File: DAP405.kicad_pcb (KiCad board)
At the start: 2 copper layers, 64 x 39 mm, 56 parts, among them J1 USB_B, J2 Target, J3 JTAG, U1 LT1117-3.3, U10 74LVC1G17, U11 SN74LVC1T45DBV, U12 SN74LVC1T45DBV, U13 SN74LVC1T45DBV, U14 SY6280, U2 USB3300-EZK, U3 STM32F405RGTx, U4 REF3033, U5 74LVC1G17, U6 SN74LVC1T45DBV, U7 SN74LVC1T45DBV, U8 SN74LVC1T45DBV, U9 SN74LVC1T45DBV, Y1 24M, Y2 12M

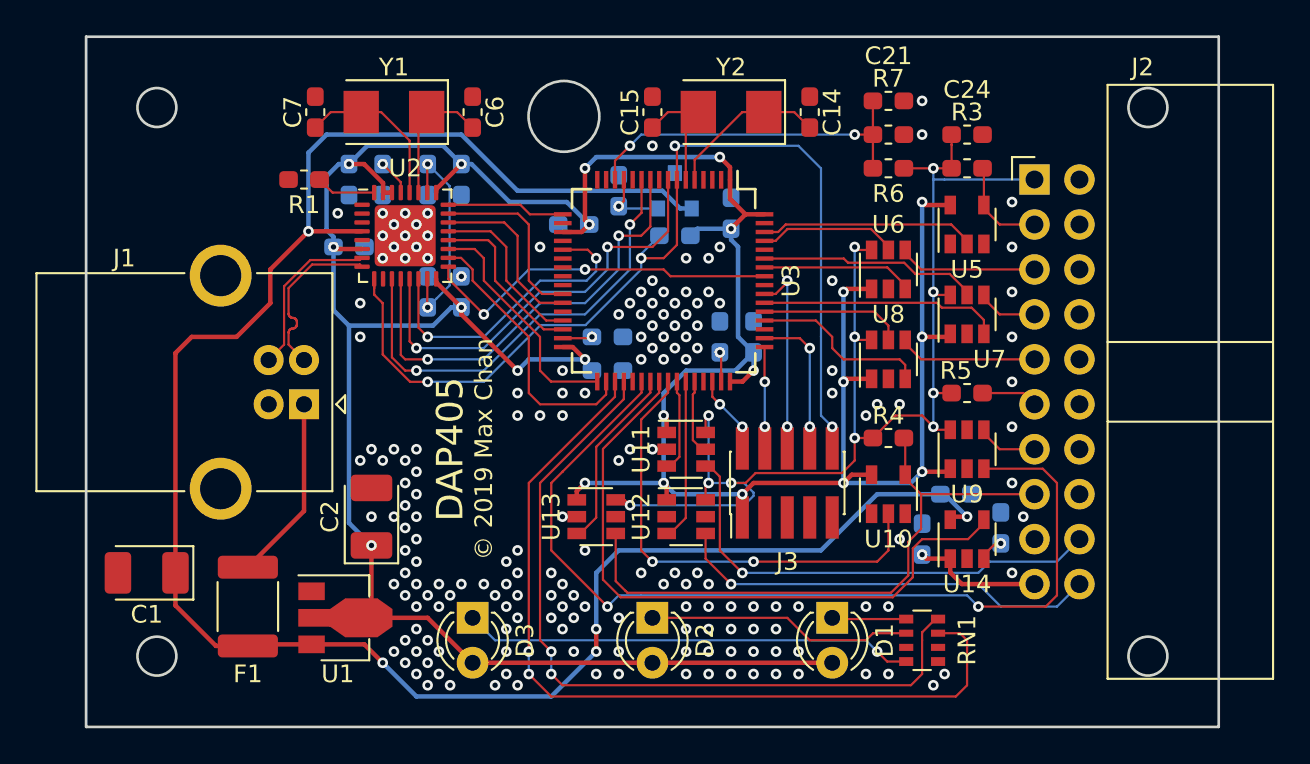
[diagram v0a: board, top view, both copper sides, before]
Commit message: Fixing the ULPI interface.
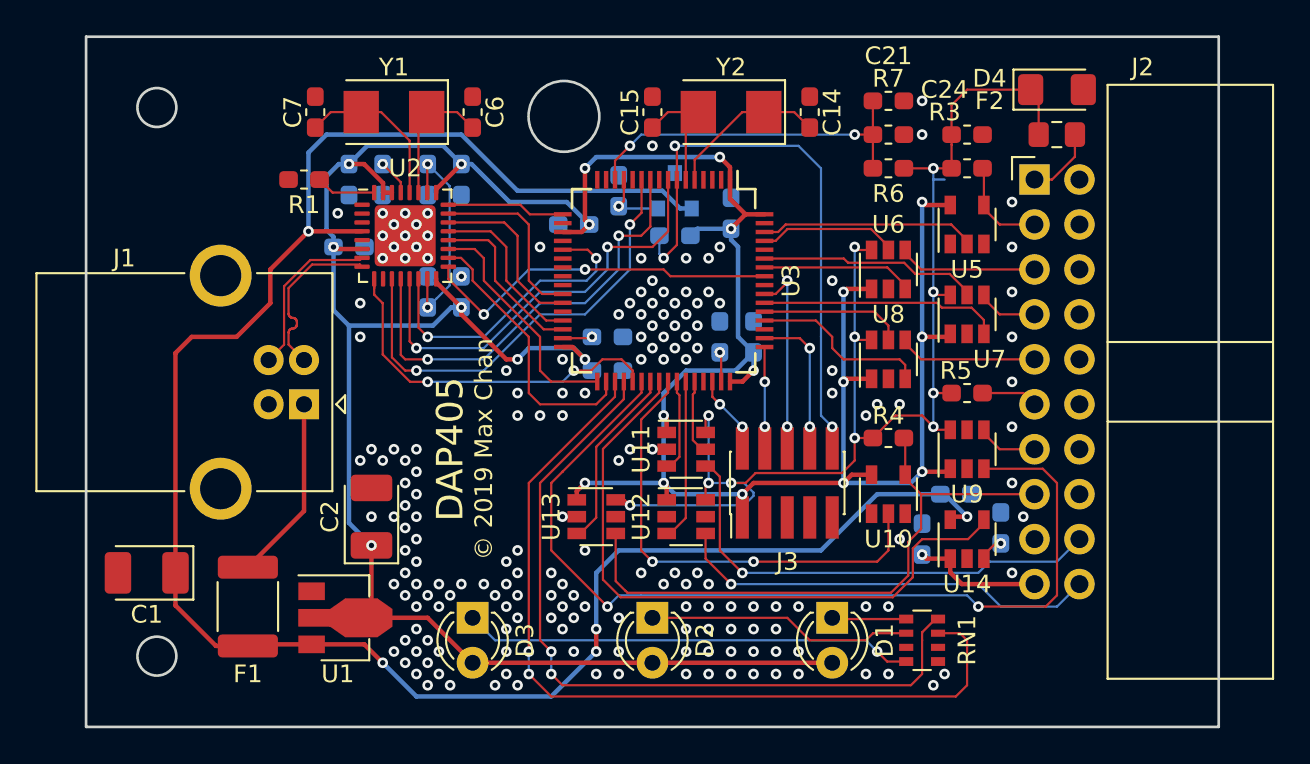
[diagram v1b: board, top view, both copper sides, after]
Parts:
- added D4: SMF5.0A, Diode_SMD:D_1206_3216Metric_Pad1.42x1.75mm_HandSolder, F.Cu at (172.9, 83.5)
- added F2: 200mA, Fuse:Fuse_0805_2012Metric_Pad1.15x1.40mm_HandSolder, F.Cu at (172.8, 86.0)
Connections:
- J2 pad 1: VDD -> Net-(F2-Pad1)
- U2 pad 9: /~RESET -> /ULPI_RST
- U3 pad 37: (no net) -> /ULPI_RST
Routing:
- net /~RESET: track 58.1 -> 33.0 mm, vias 4 -> 3
- net /ULPI_RST: track 0.00 -> 21.2 mm, vias 0 -> 2
- net VDD: track 71.8 -> 76.0 mm
- net Net-(F2-Pad1): track 0.00 -> 4.07 mm
- net GND: vias 180 -> 181
- net (no net): vias 0 -> 1
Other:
- outline, holes or cut-outs redrawn

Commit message: STM32F446 version
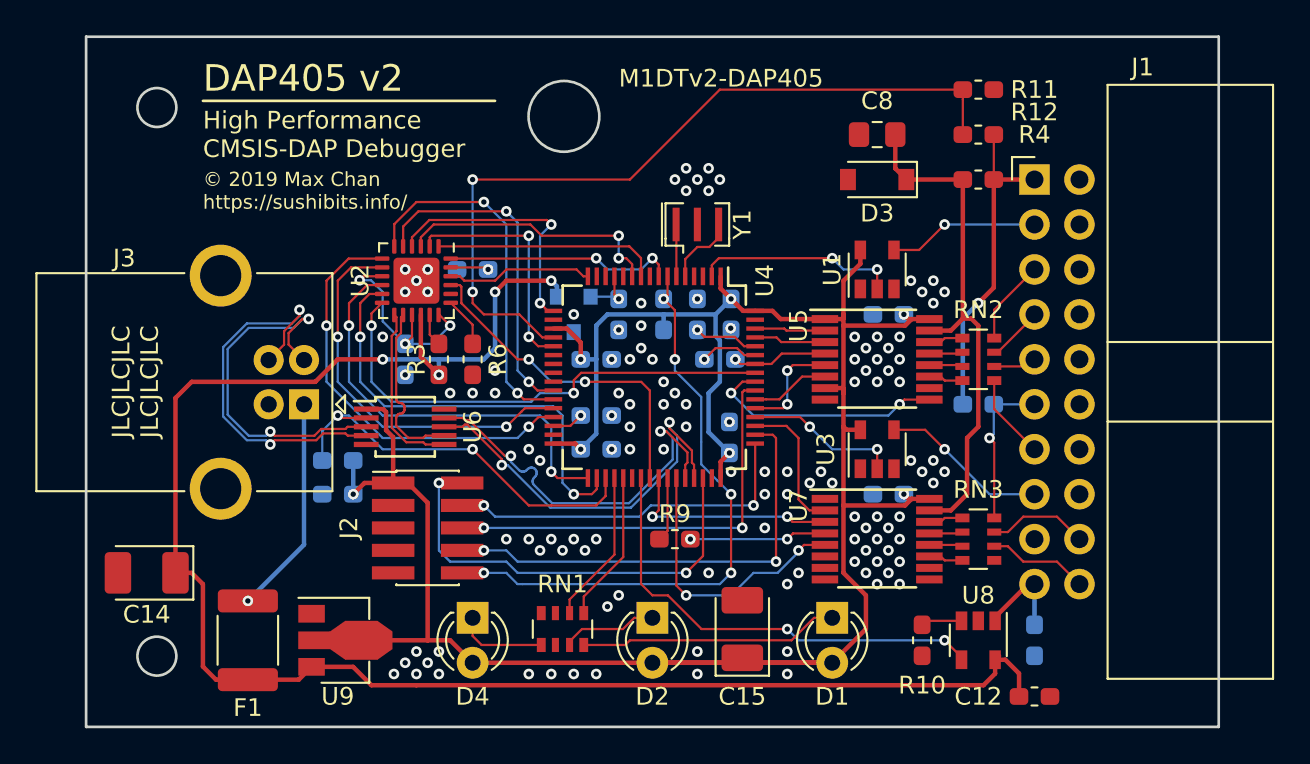
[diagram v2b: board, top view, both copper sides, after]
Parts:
- removed the C12 at (147.5, 97.5)
- removed the C13 at (153.8, 97.5)
- removed the C14 at (158.9, 84.8)
- removed the C15 at (150.0, 84.8)
- removed the C16 at (154.4, 90.5)
- removed C17, C18, C19: 100n, Capacitor_SMD:C_0603_1608Metric_Pad1.05x0.95mm_HandSolder
- removed C21, C24: 1µ, Capacitor_SMD:C_0603_1608Metric_Pad1.05x0.95mm_HandSolder
- removed the D4 at (172.9, 83.5)
- removed F2: 200mA, Fuse:Fuse_0805_2012Metric_Pad1.15x1.40mm_HandSolder
- removed the U10 at (163.3, 106.3)
- removed U11, U12, U13: SN74LVC1T45DBV, Package_TO_SOT_SMD:SOT-23-6
- removed the U8 at (163.3, 98.7)
- removed the U9 at (167.8, 103.8)
- removed Y2: 12M, Crystal:Crystal_SMD_5032-2Pin_5.0x3.2mm
- added C1: 1µ, Capacitor_SMD:C_0603_1608Metric_Pad1.05x0.95mm_HandSolder, B.Cu at (136.0, 98.7)
- added C2: 1µ, Capacitor_SMD:C_0603_1608Metric_Pad1.05x0.95mm_HandSolder, B.Cu at (139.8, 93.7)
- added D3: BZT52C3V3, Diode_SMD:D_SOD-123, F.Cu at (162.7, 88.6)
- added R11: 20k, Resistor_SMD:R_0603_1608Metric_Pad1.05x0.95mm_HandSolder, F.Cu at (168.4, 86.0)
- added R12: 30k, Resistor_SMD:R_0603_1608Metric_Pad1.05x0.95mm_HandSolder, F.Cu at (168.4, 83.5)
- added R8: 510, Resistor_SMD:R_0603_1608Metric_Pad1.05x0.95mm_HandSolder, B.Cu at (153.8, 98.7)
- added R9: 510, Resistor_SMD:R_0603_1608Metric_Pad1.05x0.95mm_HandSolder, F.Cu at (151.3, 108.9)
- added RN2: 220, Resistor_SMD:R_Array_Convex_4x0603, F.Cu at (168.4, 98.7)
- added RN3: 220, Resistor_SMD:R_Array_Convex_4x0603, F.Cu at (168.4, 108.9)
- added U1: 74LVC1G07, Package_TO_SOT_SMD:SOT-23-5, F.Cu at (162.7, 93.7)
- added U4: STM32F446RCTx, Package_QFP:LQFP-64_10x10mm_P0.5mm, F.Cu at (150.1, 99.7)
- C12: renamed from C22; moved to F.Cu
- C3: value 100n -> 4.7µ
- C6, C7: value 22p -> 100n; moved to B.Cu
- C8: value 100n -> 10µ; footprint Capacitor_SMD:C_0603_1608Metric_Pad1.05x0.95mm_HandSolder -> Capacitor_SMD:C_0805_2012Metric_Pad1.15x1.40mm_HandSolder; moved to F.Cu
- J3: renamed from J1; value USB_B -> USB
- R1: value 12k -> 10k; moved to B.Cu
- R10: renamed from R8; moved to F.Cu
- R4: value 10k -> 220
- R5: moved to B.Cu
- R6: value 20k -> 8.06k
- R7: value 30k -> 10k; moved to B.Cu
- U2: value USB3300-EZK -> USB3343; footprint Package_DFN_QFN:QFN-32-1EP_5x5mm_P0.5mm_EP3.45x3.45mm -> Package_DFN_QFN:QFN-24-1EP_4x4mm_P0.5mm_EP2.6x2.6mm
- U3: value STM32F405RGTx -> 74LVC1G07; footprint Package_QFP:LQFP-64_10x10mm_P0.5mm -> Package_TO_SOT_SMD:SOT-23-5
- U5: value 74LVC1G17 -> SN74AVC4T774; footprint Package_TO_SOT_SMD:SOT-23-5 -> Package_SO:TSSOP-16_4.4x5mm_P0.65mm
- U6: value SN74LVC1T45DBV -> FSUSB42MUX; footprint Package_TO_SOT_SMD:SOT-23-6 -> Package_SO:MSOP-10_3x3mm_P0.5mm
- U7: value SN74LVC1T45DBV -> SN74AVC4T774; footprint Package_TO_SOT_SMD:SOT-23-6 -> Package_SO:TSSOP-16_4.4x5mm_P0.65mm
- Y1: value 24M -> 16M; footprint Crystal:Crystal_SMD_5032-2Pin_5.0x3.2mm -> Crystal:Resonator_SMD_muRata_CSTxExxV-3Pin_3.0x1.1mm
- moved R7 37.2 mm to (132.2, 104.4), turned to 0 degrees
- moved C11 35.3 mm to (163.3, 106.3), turned to 180 degrees
- moved R3 31.7 mm to (137.9, 98.7), turned to 270 degrees
- moved C8 30.5 mm to (162.7, 86.0)
- moved C7 29.8 mm to (154.3, 103.1)
- moved U6 28.7 mm to (136.0, 102.5), turned to 0 degrees
- moved R6 25.9 mm to (139.8, 98.7), turned to 270 degrees
- moved C10 25.3 mm to (163.3, 96.2), turned to 180 degrees
- moved C15 21.9 mm to (155.1, 114.0)
- moved R1 21.7 mm to (150.6, 96.2), turned to 90 degrees
- moved J2 20.5 mm to (137.3, 108.3), turned to 0 degrees
- moved RN1 20.3 mm to (144.9, 114.0), turned to 90 degrees
- moved C6 20.3 mm to (146.8, 103.8), turned to 0 degrees
- moved Y1 18.3 mm to (152.5, 91.1), turned to 0 degrees
- moved C4 17.2 mm to (154.4, 96.2)
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- renumbered C23 to C13, C1 to C14, C2 to C15, C20 to C16, D3 to D4, J2 to J1, J3 to J2, U4 to U10, U14 to U8, U1 to U9
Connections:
- C3 pad 1: GND -> Net-(C3-Pad1)
- C3 pad 2: Net-(C3-Pad2) -> GND
- C4 pad 1: GND -> +3V3
- C4 pad 2: Net-(C3-Pad2) -> GND
- C5 pad 1: GND -> +3V3
- C5 pad 2: Net-(C5-Pad2) -> GND
- C6 pad 1: Net-(C6-Pad1) -> +3V3
- C7 pad 1: Net-(C7-Pad1) -> +3V3
- C8 pad 1: +3V3 -> GND
- C8 pad 2: GND -> VDD
- D4 pad 1: Net-(D3-Pad1) -> Net-(D4-Pad1)
- J1 pad 1: Net-(F2-Pad1) -> /T_VTGT
- J1 pad 15: /T_~RESET -> /T_~SRST
- R1 pad 1: Net-(R1-Pad1) -> +3V3
- R1 pad 2: GND -> /~RESET
- R2 pad 1: +3V3 -> Net-(R2-Pad1)
- R2 pad 2: /~RESET -> GND
- R3 pad 1: VDD -> Net-(R3-Pad1)
- R3 pad 2: /T_~TRST -> +5V
- R4 pad 2: /T_~RESET -> /T_VTGT
- R5 pad 1: VDD -> /T_VTGT
- R6 pad 1: VDD -> Net-(R6-Pad1)
- R6 pad 2: Net-(C21-Pad1) -> GND
- R7 pad 1: GND -> /USEL
- R7 pad 2: Net-(C21-Pad1) -> +3V3
- RN1 pad 1: Net-(D1-Pad1) -> Net-(D4-Pad1)
- RN1 pad 2: Net-(D2-Pad1) -> (no net)
- RN1 pad 3: (no net) -> Net-(D2-Pad1)
- RN1 pad 4: Net-(D3-Pad1) -> Net-(D1-Pad1)
- RN1 pad 5: GND -> /LED_ACT
- RN1 pad 6: GND -> /LED_CON
- RN1 pad 7: /LED_CON -> GND
- RN1 pad 8: /LED_ACT -> GND
- U2 pad 1: GND -> /ULPI_DIR
- U2 pad 10: (no net) -> /ULPI_D5
- U2 pad 11: /ULPI_NXT -> /ULPI_D6
- U2 pad 12: /ULPI_DIR -> /ULPI_D7
- U2 pad 13: /ULPI_STP -> /UHS_D+
- U2 pad 14: /ULPI_CLK -> /UHS_D-
- U2 pad 15: Net-(C3-Pad2) -> Net-(C1-Pad1)
- U2 pad 16: +3V3 -> +5V
- U2 pad 17: /ULPI_D7 -> Net-(R3-Pad1)
- U2 pad 18: /ULPI_D6 -> Net-(C1-Pad1)
- U2 pad 19: /ULPI_D5 -> Net-(R6-Pad1)
- U2 pad 2: GND -> /ULPI_CLK
- U2 pad 20: /ULPI_D4 -> (no net)
- U2 pad 21: /ULPI_D3 -> /ULPI_MCLK
- U2 pad 22: /ULPI_D2 -> /ULPI_~RST
- U2 pad 23: /ULPI_D1 -> Net-(C2-Pad1)
- U2 pad 24: /ULPI_D0 -> /ULPI_STP
- U2 pad 25: +3V3 -> GND
- U2 pad 3: (no net) -> /ULPI_NXT
- U2 pad 4: +5V -> /ULPI_D0
- U2 pad 5: (no net) -> /ULPI_D1
- U2 pad 6: +3V3 -> /ULPI_D2
- U2 pad 7: /D+ -> /ULPI_D3
- U2 pad 8: /D- -> /ULPI_D4
- U2 pad 9: /ULPI_RST -> Net-(C1-Pad1)
- U3 pad 1: +3V3 -> (no net)
- U3 pad 2: (no net) -> /D_~SRST
- U3 pad 3: (no net) -> GND
- U3 pad 4: (no net) -> /T_~SRST
- U3 pad 5: Net-(C14-Pad1) -> +3V3
- U5 pad 1: (no net) -> +3V3
- U5 pad 2: /D_~TRST -> /R_TMS
- U5 pad 3: GND -> /D_TDI
- U5 pad 4: /T_~TRST -> /D_TMS
- U5 pad 5: +3V3 -> /D_TCK
- U6 pad 2: GND -> /USEL
- U6 pad 3: /D_TDI -> /D-
- U6 pad 4: /T_TDI -> /D+
- U6 pad 5: /OE_TDI -> GND
- U6 pad 6: VDD -> /UHS_D+
- U7 pad 1: +3V3 -> GND
- U7 pad 2: GND -> /R_TXD
- U7 pad 3: /D_TMS -> /D_RTCK
- U7 pad 4: /T_TMS -> /D_TXD
- U7 pad 5: /OE_TMS -> /D_RXD
- U7 pad 6: VDD -> (no net)
- Y1 pad 1: Net-(C6-Pad1) -> Net-(U4-Pad6)
- Y1 pad 2: Net-(C7-Pad1) -> GND
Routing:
- net +3V3: track 204.6 -> 139.4 mm, vias 22 -> 7
- net /D_TDO: track 53.1 -> 4.48 mm, vias 2 -> 0
- net VDD: track 76.0 -> 29.4 mm, vias 11 -> 0
- net /D_VTGT: track 0.00 -> 44.7 mm, vias 0 -> 2
- net /LED_CON: track 48.4 -> 8.68 mm, vias 2 -> 0
- net /LED_ACT: track 43.8 -> 8.56 mm, vias 2 -> 0
- net /T_~RESET: track 34.8 -> 0.00 mm
- net /D_~RESET: track 26.7 -> 0.00 mm, vias 2 -> 0
- net Net-(D3-Pad1): track 25.5 -> 0.00 mm, vias 1 -> 0
- net /USEL: track 0.00 -> 23.0 mm, vias 0 -> 2
- net /UFS_D-: track 0.00 -> 22.6 mm, vias 0 -> 2
- net /UFS_D+: track 0.00 -> 22.6 mm, vias 0 -> 2
- net /ULPI_RST: track 21.2 -> 0.00 mm, vias 2 -> 0
- net /T_TXD: track 26.9 -> 5.70 mm, vias 1 -> 0
- net /TMS: track 4.48 -> 25.4 mm
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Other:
- board text added: "DAP405 v2"
- board text added: "High Performance CMSIS-DAP Debugger"
- board text added: "JLCJLCJLC JLCJLCJLC"
- board text added: "M1DTv2-DAP405"
- board text added: "© 2019 Max Chan https://sushibits.info/"
- board text removed: "DAP405"
- board text removed: "© 2019 Max Chan"
